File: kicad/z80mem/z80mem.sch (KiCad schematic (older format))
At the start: 6 parts, among them U1 MS628128, U2 2764, U3 z80pcb, U4 74LS32, U6 7400, U7 74LS138

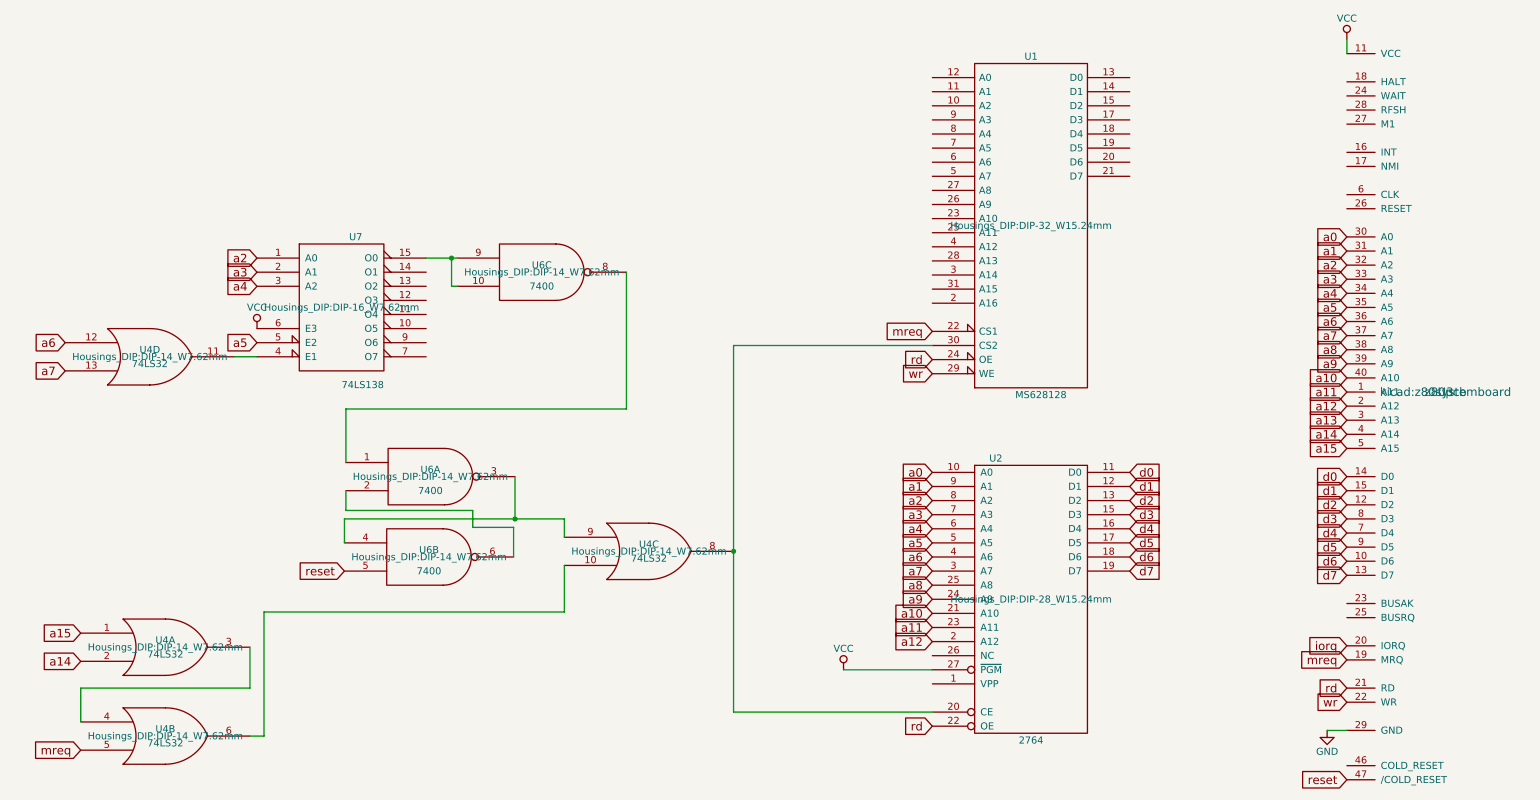
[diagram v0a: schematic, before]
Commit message: add some unfished pcbs
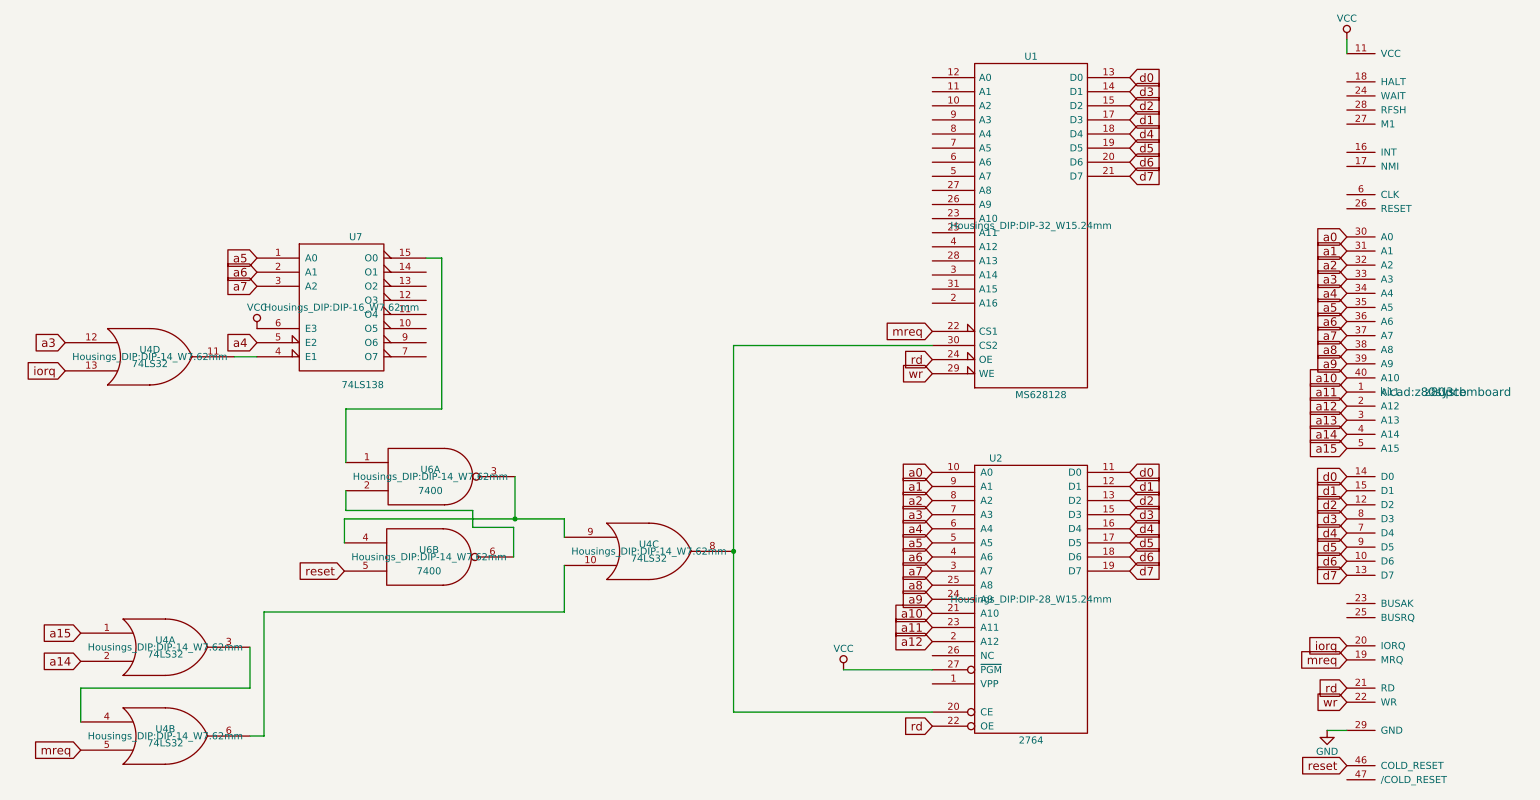
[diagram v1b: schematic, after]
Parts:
- removed unit 3 of U6
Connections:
- net a2: no longer U7.1 (A0)
- net a3: now also U4.12; no longer U7.2 (A1)
- net a4: now also U7.5 (E2); no longer U7.3 (A2)
- net a5: now also U7.1 (A0); no longer U7.5 (E2)
- net a6: now also U7.2 (A1); no longer U4.12
- net a7: now also U7.3 (A2); no longer U4.13
- net d0: now also U1.13 (D0)
- net d1: now also U1.17 (D3)
- net d2: now also U1.15 (D2)
- net d3: now also U1.14 (D1)
- net d4: now also U1.18 (D4)
- net d5: now also U1.19 (D5)
- net d6: now also U1.20 (D6)
- net d7: now also U1.21 (D7)
- net iorq: now also U4.13
- net reset: now also U3.46 (COLD_RESET); no longer U3.47 (/COLD_RESET)
- net at U6.1: now also U7.15 (O0)
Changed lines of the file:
@@
 Text GLabel 9850 3900 0    60   Input ~ 0
 a15
-Text GLabel 6910 4070 0    60   Input ~ 0
-a0
-Text GLabel 6910 4170 0    60   Input ~ 0
-a1
-Text GLabel 6910 4270 0    60   Input ~ 0
-a2
-Text GLabel 6910 4370 0    60   Input ~ 0
-a3
-Text GLabel 6910 4470 0    60   Input ~ 0
-a4
-Text GLabel 6910 4570 0    60   Input ~ 0
-a5
-Text GLabel 6910 4670 0    60   Input ~ 0
-a6
-Text GLabel 6910 4770 0    60   Input ~ 0
-a7
-Text GLabel 6910 4870 0    60   Input ~ 0
-a8
-Text GLabel 6910 4970 0    60   Input ~ 0
-a9
-Text GLabel 6910 5070 0    60   Input ~ 0
-a10
-Text GLabel 6910 5170 0    60   Input ~ 0
-a11
-Text GLabel 6910 5270 0    60   Input ~ 0
-a12
 $Comp
 L VCC #PWR02
@@
 $EndComp
 Text GLabel 760  3150 0    60   Input ~ 0
-a6
+a3
 Text GLabel 760  3350 0    60   Input ~ 0
-a7
+iorq
 Text GLabel 9850 5300 0    60   Input ~ 0
 iorq
@@
 Text GLabel 2740 4770 0    60   Input ~ 0
 reset
-Text GLabel 9850 6250 0    60   Input ~ 0
+Text GLabel 9850 6150 0    60   Input ~ 0
 reset
 Text GLabel 6910 3070 0    60   Input ~ 0
@@
 $EndComp
 Text GLabel 2120 3150 0    60   Input ~ 0
+a4
+Text GLabel 2120 2750 0    60   Input ~ 0
+a7
+Text GLabel 2120 2650 0    60   Input ~ 0
+a6
+Text GLabel 2120 2550 0    60   Input ~ 0
 a5
-Text GLabel 2120 2750 0    60   Input ~ 0
-a4
-Text GLabel 2120 2650 0    60   Input ~ 0
-a3
-Text GLabel 2120 2550 0    60   Input ~ 0
-a2
 $Comp
 L VCC #PWR04
@@
 	1    0    0    -1
 $EndComp
-$Comp
-L 7400 U6
-U 3 1 57546011
-P 4140 2650
-F 0 "U6" H 4140 2700 50  0000 C CNN
-F 1 "7400" H 4140 2550 50  0000 C CNN
-F 2 "Housings_DIP:DIP-14_W7.62mm" H 4140 2650 50  0000 C CNN
-F 3 "" H 4140 2650 50  0000 C CNN
-	3    4140 2650
-	1    0    0    -1
-$EndComp
 Wire Wire Line
 	9850 1000 9850 1100
@@
 	2120 3250 1960 3250
 Wire Wire Line
-	3320 2550 3540 2550
-Wire Wire Line
-	3500 2550 3500 2750
-Wire Wire Line
-	3500 2750 3540 2750
-Connection ~ 3500 2550
-Wire Wire Line
-	4740 2650 4740 3620
-Wire Wire Line
-	4740 3620 2750 3620
-Wire Wire Line
 	2750 3620 2750 4000
+Wire Wire Line
+	3320 2550 3430 2550
+Wire Wire Line
+	3430 2550 3430 3620
+Wire Wire Line
+	3430 3620 2750 3620
+Text GLabel 8310 1270 2    60   Input ~ 0
+d0
+Text GLabel 8310 1570 2    60   Input ~ 0
+d1
+Text GLabel 8310 1470 2    60   Input ~ 0
+d2
+Text GLabel 8310 1370 2    60   Input ~ 0
+d3
+Text GLabel 8310 1670 2    60   Input ~ 0
+d4
+Text GLabel 8310 1770 2    60   Input ~ 0
+d5
+Text GLabel 8310 1870 2    60   Input ~ 0
+d6
+Text GLabel 8310 1970 2    60   Input ~ 0
+d7
+Text GLabel 6910 5270 0    60   Input ~ 0
+a12
+Text GLabel 6910 5170 0    60   Input ~ 0
+a11
+Text GLabel 6910 5070 0    60   Input ~ 0
+a10
+Text GLabel 6910 4970 0    60   Input ~ 0
+a9
+Text GLabel 6910 4870 0    60   Input ~ 0
+a8
+Text GLabel 6910 4770 0    60   Input ~ 0
+a7
+Text GLabel 6910 4670 0    60   Input ~ 0
+a6
+Text GLabel 6910 4570 0    60   Input ~ 0
+a5
+Text GLabel 6910 4470 0    60   Input ~ 0
+a4
+Text GLabel 6910 4370 0    60   Input ~ 0
+a3
+Text GLabel 6910 4270 0    60   Input ~ 0
+a2
+Text GLabel 6910 4170 0    60   Input ~ 0
+a1
+Text GLabel 6910 4070 0    60   Input ~ 0
+a0
 $EndSCHEMATC
